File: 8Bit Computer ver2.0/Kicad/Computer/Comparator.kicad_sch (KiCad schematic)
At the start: 9 parts, among them IC146 SN74LVC1G14DBVR, IC147 SN74HC682N, IC148 SN74AHC08DR, IC149 SN74HCS4075DR, IC150 SN74AHC74DR, IC151 SN74LVC1G14DBVR, IC152 SN74LVC1G14DBVR, IC153 SN74LVC1G08DBVR, IC154 SN74ABT574ADWR

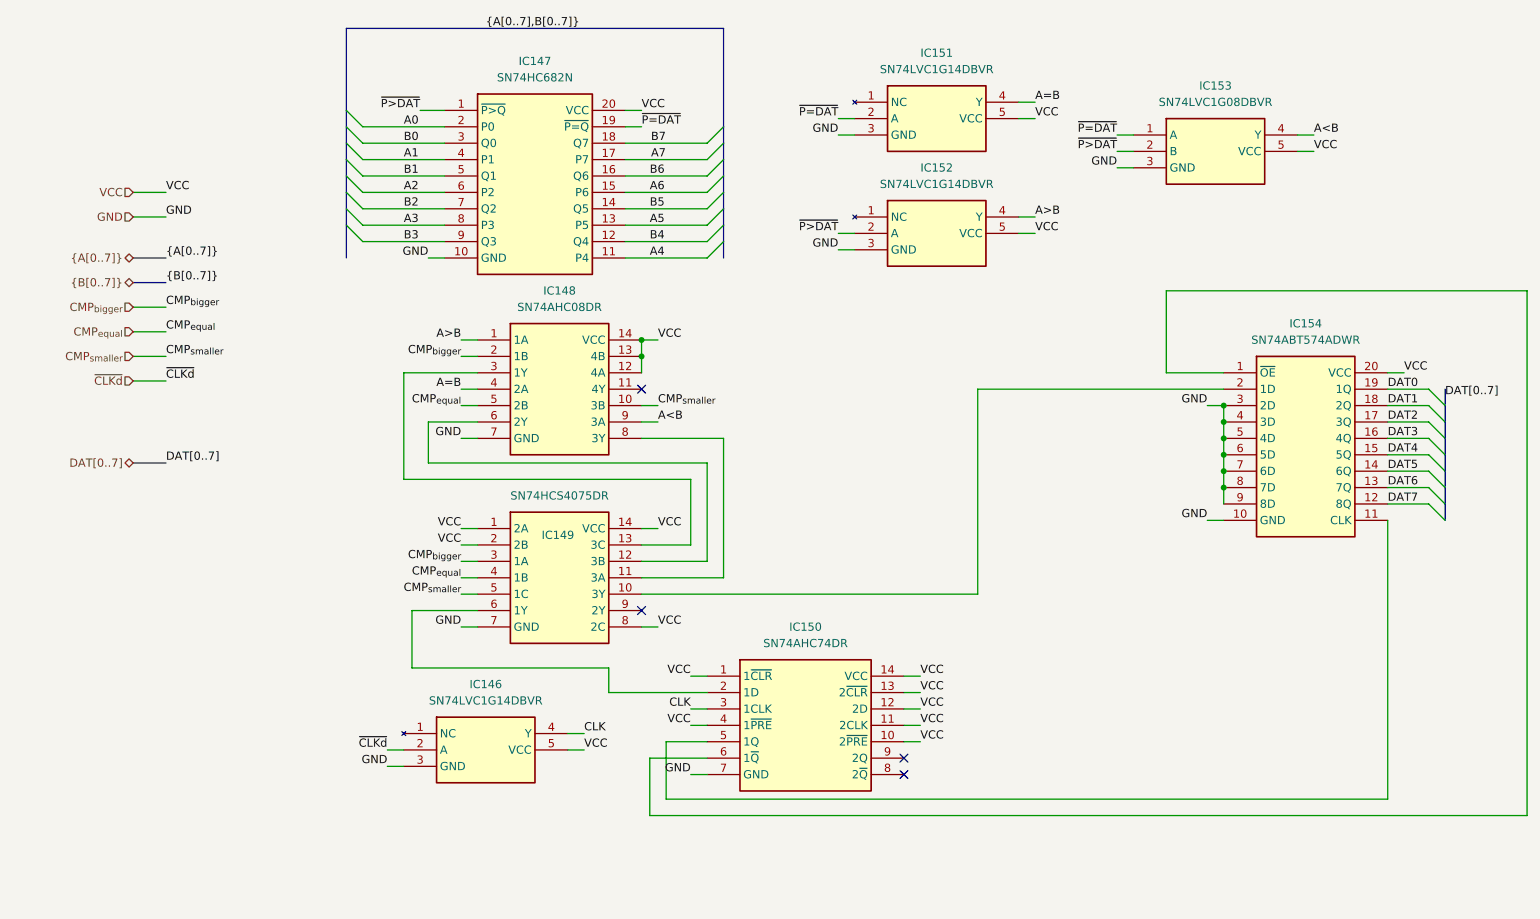
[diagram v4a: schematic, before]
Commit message: part 1 of changing to A4
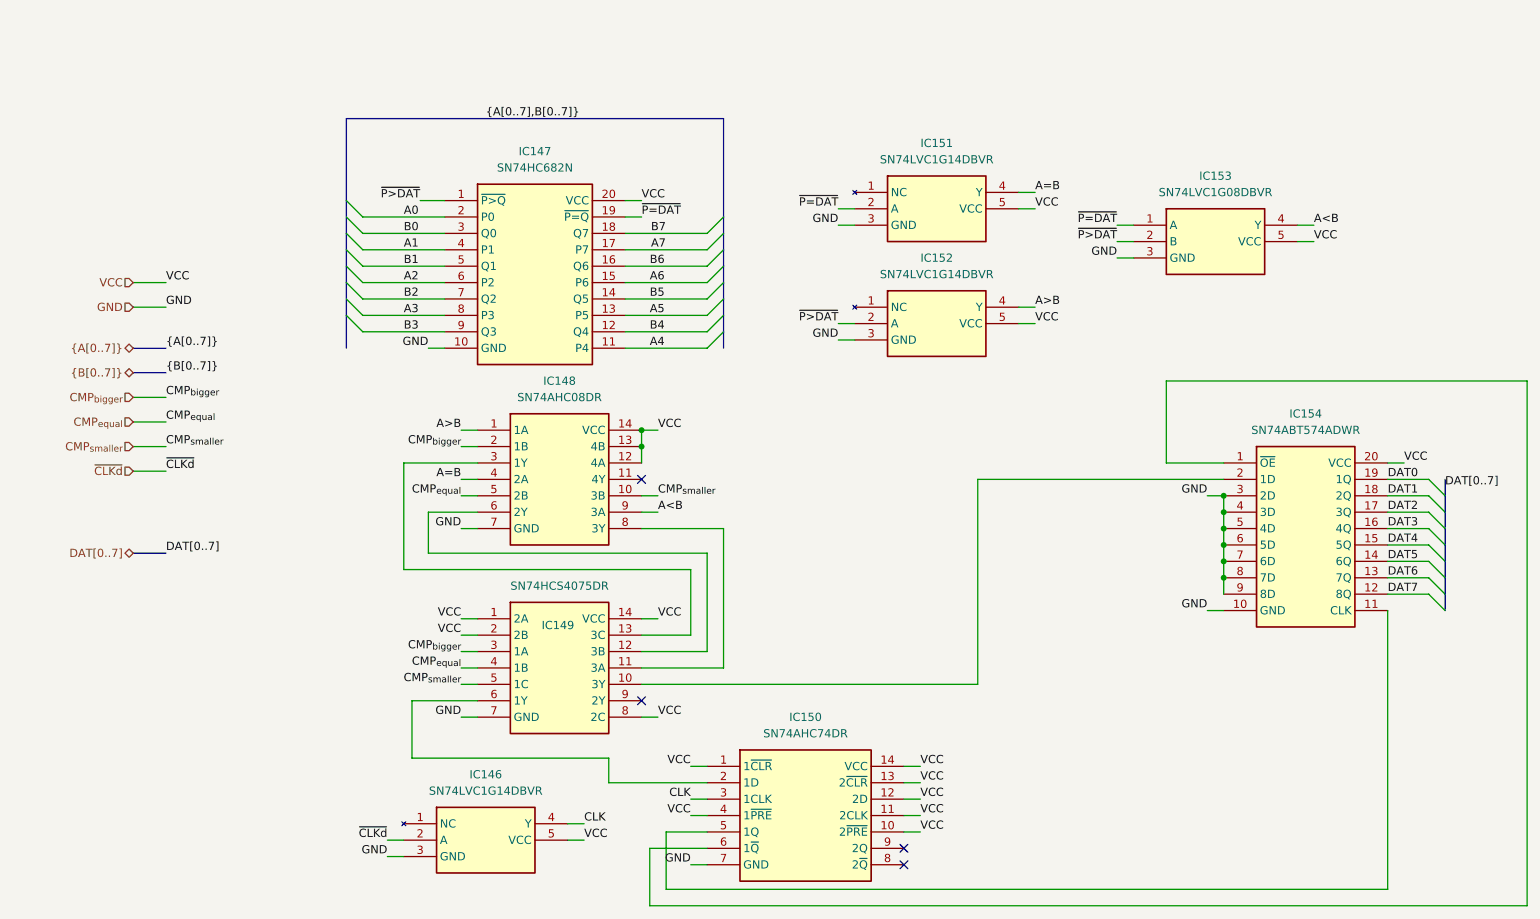
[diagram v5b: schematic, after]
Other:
- moved on the sheet: IC146, IC147, IC148, IC149, IC150, IC151, IC152, IC153, IC154

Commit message: changed page numbers, every schematic is now A4
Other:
- title: (none) -> ${SHEETNAME}
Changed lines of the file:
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@@
 	(generator_version "9.0")
 	(paper "A4")
+	(title_block
+		(title "${SHEETNAME}")
+		(date "2026-03-21")
+		(rev "2.7")
+	)
 	(junction
 		(at 204.47 88.9)
